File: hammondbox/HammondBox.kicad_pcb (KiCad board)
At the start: 2 copper layers, 42.5 x 29 mm, 14 parts, among them P1 USB_OTG, P2 CONN_02X03, P3 CONN_01X08, U1 ESP-12E, U2 TLV70233DBV

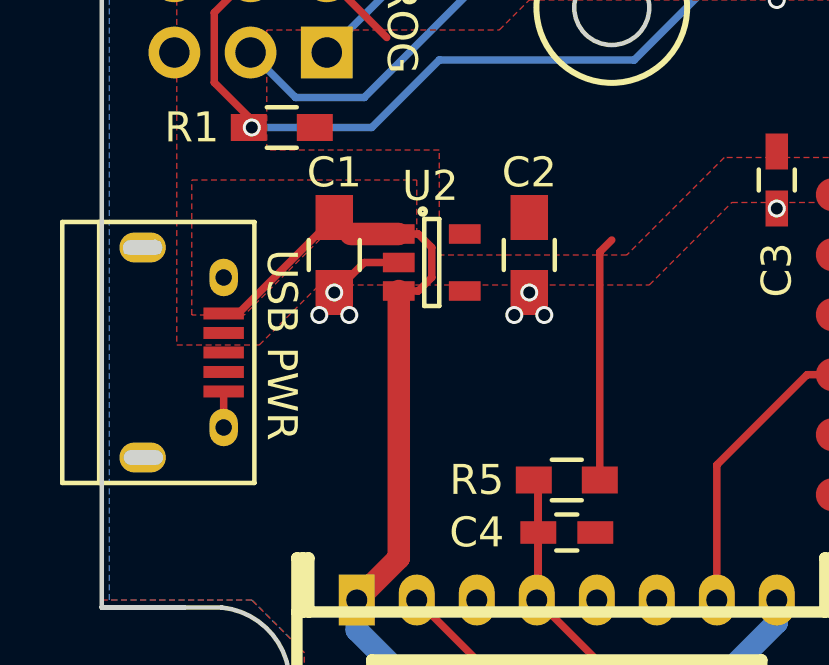
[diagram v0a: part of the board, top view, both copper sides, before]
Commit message: Increase 5v zone size
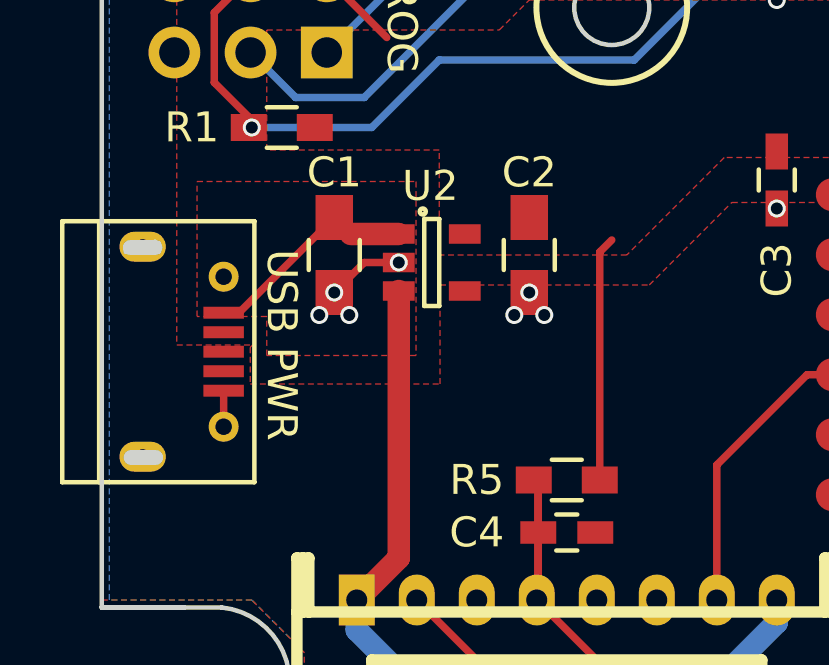
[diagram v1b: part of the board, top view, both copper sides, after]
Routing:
- net +5V: track 38.9 -> 35.4 mm
- net GND: vias 9 -> 10
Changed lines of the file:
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@@
   (general
     (links 42)
-    (no_connects 1)
+    (no_connects 3)
     (area 96.575 49.141666 149.426201 81.71954)
     (thickness 1.6)
     (drawings 26)
-    (tracks 120)
+    (tracks 116)
     (zones 0)
     (modules 14)
@@
     (mod_text_size 1 1)
     (mod_text_width 0.15)
-    (pad_size 1.55 1)
-    (pad_drill 0.5)
+    (pad_size 1 1)
+    (pad_drill 0.55)
     (pad_to_mask_clearance 0.2)
     (aux_axis_origin 100 79)
     (grid_origin 100 50)
-    (visible_elements FFFFFF6F)
+    (visible_elements FFFEFF7F)
     (pcbplotparams
       (layerselection 0x010f0_ffffffff)
@@
   )
   (module Connect:USB_Micro-B (layer F.Cu)
-    (at 102.5 64.25 270)
+    (at 102.5 64.225 270)
     (descr "Micro USB Type B Receptacle")
     (tags "USB USB_B USB_micro USB_OTG")
@@
     (pad 5 smd rect (at 1.2991 -1.56254) (size 1.35 0.4) (layers F.Cu F.Paste F.Mask)
       (net 1 GND))
-    (pad 6 thru_hole oval (at -2.5009 -1.56254) (size 0.95 1.25) (drill 0.55) (layers *.Cu *.Mask F.SilkS)
-      (net 1 GND))
-    (pad 6 thru_hole oval (at 2.4991 -1.56254) (size 0.95 1.25) (drill 0.55) (layers *.Cu *.Mask F.SilkS)
+    (pad 6 thru_hole circle (at -2.5009 -1.56254) (size 1 1) (drill 0.55) (layers *.Cu *.Mask F.SilkS)
+      (net 1 GND))
+    (pad 6 thru_hole circle (at 2.4991 -1.56254) (size 1 1) (drill 0.55) (layers *.Cu *.Mask F.SilkS)
       (net 1 GND))
     (pad 6 thru_hole oval (at -3.5009 1.13746) (size 1.55 1) (drill 0.5) (layers *.Cu *.Mask F.SilkS)
@@
   (gr_line (start 100.8 60.9) (end 100.8 60.7) (angle 90) (layer Edge.Cuts) (width 0.15))
   (gr_line (start 101.9 60.6) (end 101.9 60.9) (angle 90) (layer Edge.Cuts) (width 0.15))
-  (gr_text "ESP HammondBox 0.1" (at 141.25 64.25 90) (layer B.SilkS)
-    (effects (font (size 1.5 1.5) (thickness 0.3)) (justify mirror))
-  )
-  (gr_text z2amiller (at 101.25 64.25 270) (layer B.SilkS)
+  (gr_text "ESP HammondBox 0.1" (at 129.8 51.475 180) (layer B.SilkS)
+    (effects (font (size 1.25 1.25) (thickness 0.3)) (justify mirror))
+  )
+  (gr_text z2amiller (at 115.325 77.5) (layer B.SilkS)
     (effects (font (size 1.5 1.5) (thickness 0.3)) (justify mirror))
   )
@@
   (gr_line (start 100 50.5) (end 100 50) (angle 90) (layer Edge.Cuts) (width 0.15))
   (gr_line (start 142.5 79) (end 142.5 50.5) (angle 90) (layer Edge.Cuts) (width 0.15))
+  (via (at 109.9 61.25) (size 0.6) (drill 0.4) (layers F.Cu B.Cu) (net 1) (status C00000))
   (segment (start 104.06254 65.5491) (end 104.06254 66.7491) (width 0.25) (layer F.Cu) (net 1))
   (via (at 122.5 59.45) (size 0.6) (drill 0.4) (layers F.Cu B.Cu) (net 1))
@@
   (segment (start 109.9 62.2) (end 109.9 71.09976) (width 0.75) (layer F.Cu) (net 2))
   (segment (start 109.9 71.09976) (end 108.49976 72.5) (width 0.75) (layer F.Cu) (net 2))
-  (segment (start 109.9 60.3) (end 110.55 60.3) (width 0.25) (layer F.Cu) (net 2))
-  (segment (start 110.55 62.2) (end 109.9 62.2) (width 0.25) (layer F.Cu) (net 2))
-  (segment (start 111 61.75) (end 110.55 62.2) (width 0.25) (layer F.Cu) (net 2))
-  (segment (start 111 60.75) (end 111 61.75) (width 0.25) (layer F.Cu) (net 2))
-  (segment (start 110.55 60.3) (end 111 60.75) (width 0.25) (layer F.Cu) (net 2))
   (segment (start 104.06254 62.9491) (end 104.5509 62.9491) (width 0.25) (layer F.Cu) (net 2))
   (segment (start 104.5509 62.9491) (end 107.75 59.75) (width 0.25) (layer F.Cu) (net 2))
@@
     )
   )
+  (zone (net 1) (net_name GND) (layer F.Cu) (hatch edge 0.508)
+    (connect_pads (clearance 0.1))
+    (min_thickness 0.1)
+    (fill yes (arc_segments 16) (thermal_gap 0.508) (thermal_bridge_width 0.508))
+    (polygon
+      (pts
+        (xy 102.5 64) (xy 105.025 64) (xy 104.95 64.075) (xy 104.95 65.3) (xy 111.275 65.3)
+        (xy 111.275 62) (xy 118.25 62) (xy 121 59.25) (xy 128.75 59.25) (xy 128.75 50.25)
+        (xy 142.25 50.25) (xy 142.25 78.75) (xy 106.75 78.75) (xy 106.75 74.25) (xy 105 72.5)
+        (xy 100 72.5) (xy 100 50.25) (xy 102.5 50.25) (xy 102.5 64)
+      )
+    )
+  )
   (zone (net 2) (net_name +5V) (layer F.Cu) (hatch edge 0.508)
     (connect_pads yes (clearance 0.1))
@@
     (polygon
       (pts
-        (xy 110.5 60.25) (xy 107.5 60.25) (xy 104.75 63) (xy 103 63) (xy 103 58.5)
-        (xy 110.5 58.5) (xy 110.5 60.25)
+        (xy 110.475 64.35) (xy 105.5 64.35) (xy 105.5 63.05) (xy 103.175 63.05) (xy 103.175 58.55)
+        (xy 110.475 58.55) (xy 110.475 64.35)
       )
     )
-  )
-  (zone (net 1) (net_name GND) (layer F.Cu) (hatch edge 0.508)
-    (connect_pads (clearance 0.1))
-    (min_thickness 0.1)
-    (fill yes (arc_segments 16) (thermal_gap 0.508) (thermal_bridge_width 0.508))
-    (polygon
-      (pts
-        (xy 102.5 64) (xy 105.25 64) (xy 107.25 62) (xy 118.25 62) (xy 121 59.25)
-        (xy 128.75 59.25) (xy 128.75 50.25) (xy 142.25 50.25) (xy 142.25 78.75) (xy 106.75 78.75)
-        (xy 106.75 74.25) (xy 105 72.5) (xy 100 72.5) (xy 100 50.25) (xy 102.5 50.25)
-        (xy 102.5 64)
-      )
-    )
